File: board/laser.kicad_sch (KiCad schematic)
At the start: 0 parts

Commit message: Final 1
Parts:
- added Conn10, Conn11: Molex_uF_D_02, MRDT_Connectors:MOLEX_uF_D_02_Horizontal, symbol MRDT_Connectors:Molex_uF_D_02
- added D4: Orange, symbol Device:LED
- added Q1: BSS138, Package_TO_SOT_SMD:SOT-23, symbol Transistor_FET:BSS138
- added R26: 2200, symbol Device:R_US
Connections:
- new net: D4.1 (K), R26.1
- new net: Conn10.2, Conn11.2, Q1.3 (D), R26.2
- new net +5V: Conn10.1, Conn11.1, D4.2 (A)
- new net GND: Q1.2 (S)
- new net LAS: Q1.1 (G)

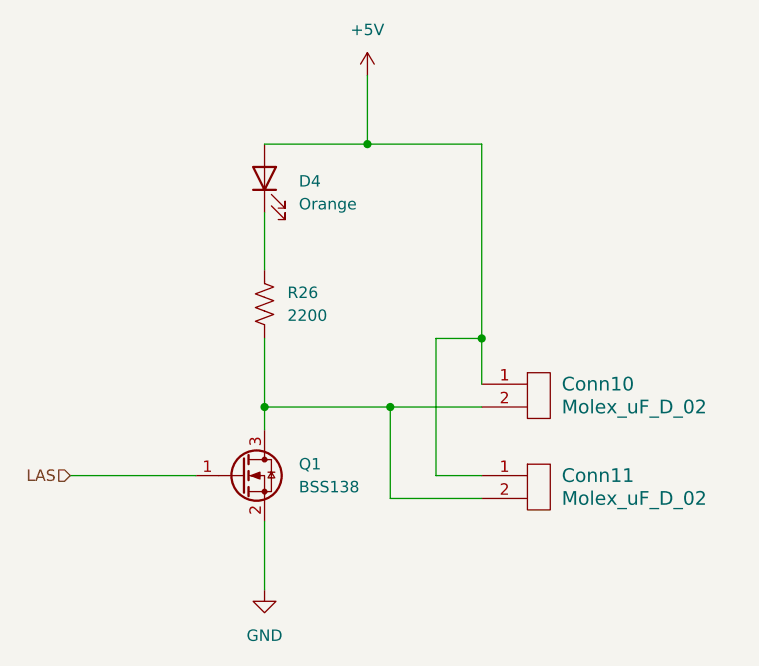
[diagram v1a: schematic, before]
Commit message: Schematic review changes
Updated molex connectors, can ics, buttons are no longer pull ups, and some appearence changes.
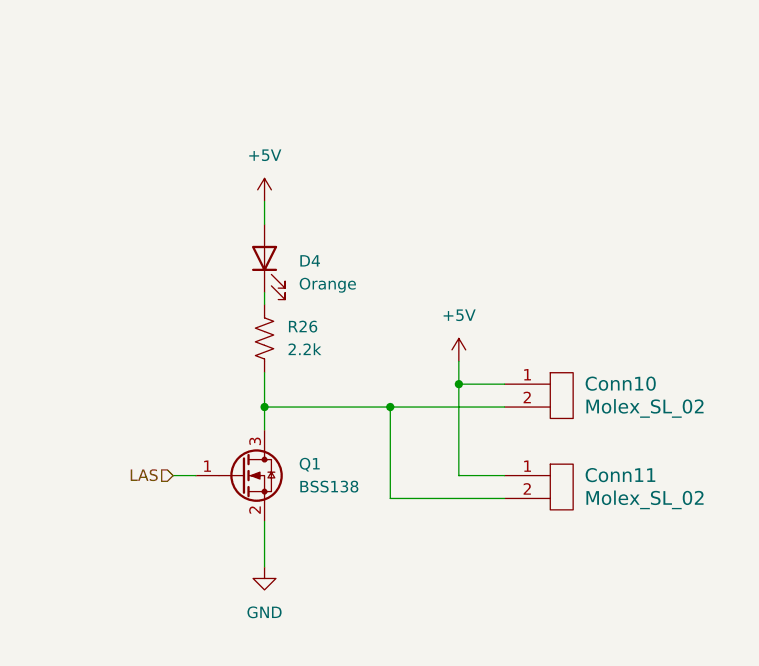
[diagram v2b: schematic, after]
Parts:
- removed Conn10, Conn11: Molex_uF_D_02, MRDT_Connectors:MOLEX_uF_D_02_Horizontal, symbol MRDT_Connectors:Molex_uF_D_02
- added Conn10, Conn11: Molex_SL_02, symbol MRDT_Connectors:Molex_SL_02
- R26: value 2200 -> 2.2k
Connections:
- net +5V: now also Conn10.1, Conn11.1
- net at Q1.3 (D), R26.2: now also Conn10.2, Conn11.2
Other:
- moved on the sheet: D4, R26

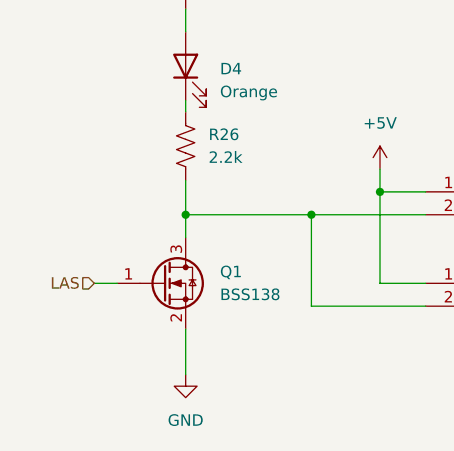
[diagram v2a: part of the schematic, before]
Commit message: Schematic review changes part 2 the electric boogaloo
finished fixing schematic. Made better names for heiracal pins. Made LED ressistors standard values.
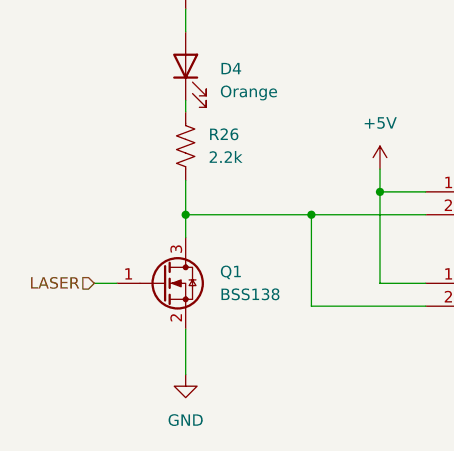
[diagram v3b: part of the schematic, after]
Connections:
- net LAS renamed LASER
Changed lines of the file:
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@@
 		)
 	)
-	(hierarchical_label "LAS"
+	(hierarchical_label "LASER"
 		(shape input)
 		(at 68.58 106.68 180)

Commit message: Prototype Layout
Made an initial Layout to be edited and changed uwu
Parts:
- Conn10, Conn11: footprint (none) -> MRDT_Connectors:MOLEX_SL_02_Vertical
- D4: footprint (none) -> LED_SMD:LED_0603_1608Metric_Pad1.05x0.95mm_HandSolder
- R26: footprint (none) -> Resistor_SMD:R_0603_1608Metric_Pad0.98x0.95mm_HandSolder
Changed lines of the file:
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@@
 			)
 		)
-		(property "Footprint" ""
+		(property "Footprint" "Resistor_SMD:R_0603_1608Metric_Pad0.98x0.95mm_HandSolder"
 			(at 79.756 91.694 90)
 			(effects
@@
 			)
 		)
-		(property "Footprint" ""
+		(property "Footprint" "LED_SMD:LED_0603_1608Metric_Pad1.05x0.95mm_HandSolder"
 			(at 78.74 82.55 0)
 			(effects
@@
 			)
 		)
-		(property "Footprint" ""
+		(property "Footprint" "MRDT_Connectors:MOLEX_SL_02_Vertical"
 			(at 110.49 113.03 0)
 			(effects
@@
 			)
 		)
-		(property "Footprint" ""
+		(property "Footprint" "MRDT_Connectors:MOLEX_SL_02_Vertical"
 			(at 110.49 102.87 0)
 			(effects
